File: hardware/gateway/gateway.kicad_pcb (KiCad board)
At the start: 2 copper layers, 65 x 32 mm, 34 parts, among them J1 FTDI, J2 Conn_Coaxial, J3 Raspberry_Pi_2_3, U1 RFM69HW, U2 MCP7940N-xSN, U3 AP130-xxY, Y1 32768 - 6pF

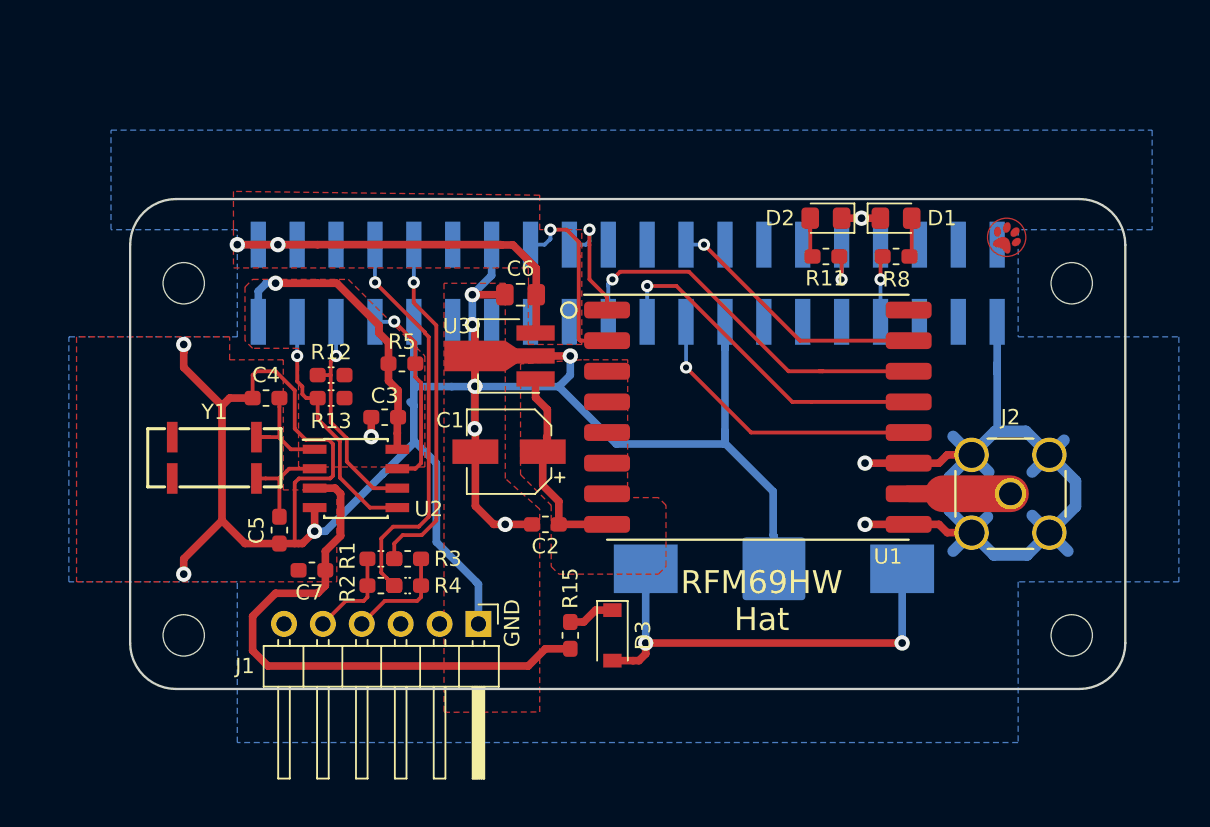
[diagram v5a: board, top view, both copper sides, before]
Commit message: DS1307 and PTH crystal
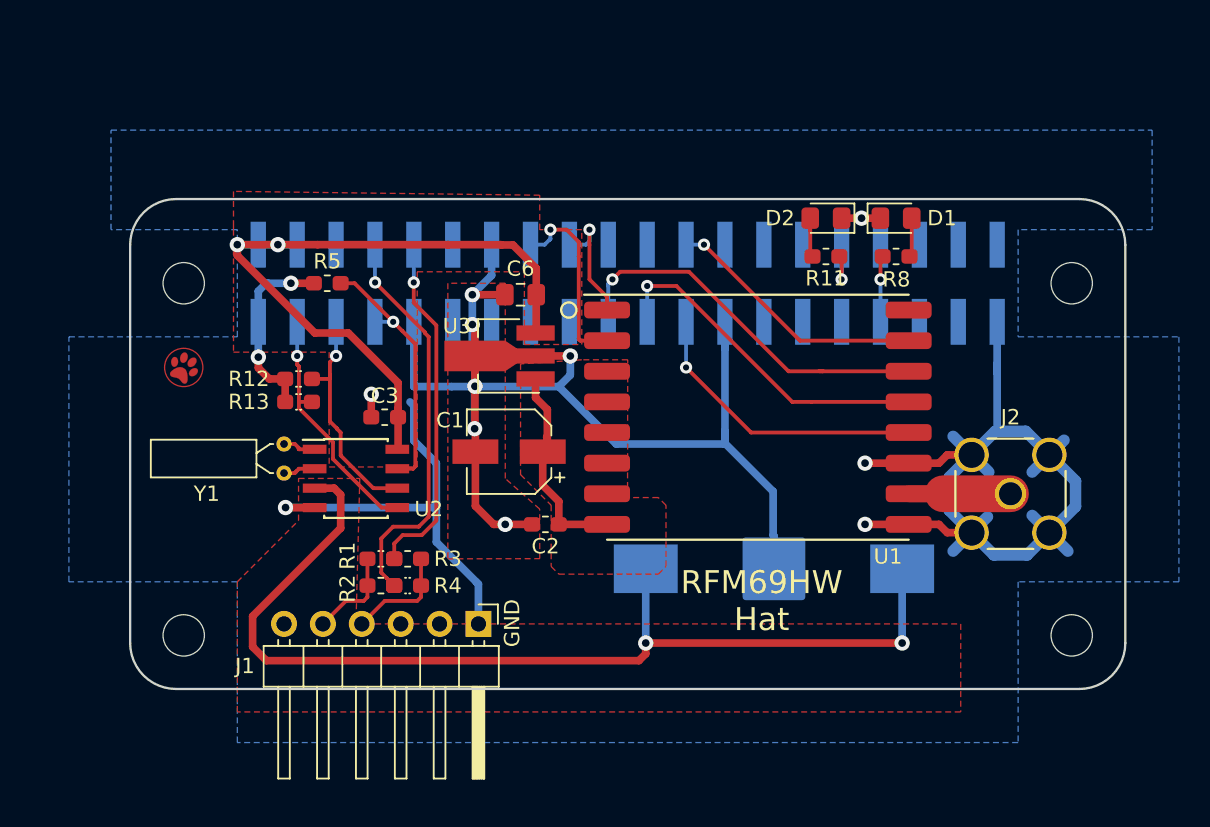
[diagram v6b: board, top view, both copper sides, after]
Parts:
- removed C4, C5: 10p, Capacitor_SMD:C_0603_1608Metric_Pad1.05x0.95mm_HandSolder
- removed C7: 100n, Capacitor_SMD:C_0603_1608Metric_Pad1.05x0.95mm_HandSolder
- removed D3: B0520LW-7-F, Diode_SMD:D_SOD-123
- removed R15: 1k, Resistor_SMD:R_0603_1608Metric_Pad1.05x0.95mm_HandSolder
- U2: value MCP7940N-xSN -> DS1307Z+
- Y1: value 32768 - 6pF -> 32768; footprint humidity:Crystal LFXTAL016178 -> Crystal:Crystal_C26-LF_D2.1mm_L6.5mm_Horizontal
- moved G*** 54.4 mm to (100.0, 55.5)
- moved R5 7.16 mm to (109.4, 50.0)
- moved Y1 4.64 mm to (106.5, 60.5), turned to 270 degrees
- moved R12 2.14 mm to (107.5, 56.2), turned to 180 degrees
- moved R13 2.14 mm to (107.5, 57.8), turned to 180 degrees
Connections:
- net /MFP renamed /RTC_SQ_OUT
- BT1 pad 1: /VBAT_IN -> /VBAT
- C3 pad 1: +3V3_PI -> +5V_PI
- U2 pad 8: +3V3_PI -> +5V_PI
- Y1 pad 1: /X2 -> /X1
- Y1 pad 2: /X1 -> /X2
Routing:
- net GND: track 226.1 -> 180.7 mm, vias 13 -> 11
- net /VBAT: track 37.7 -> 67.6 mm, vias 0 -> 2
- net /VBAT_IN: track 29.5 -> 0.00 mm, vias 2 -> 0
- net +5V_PI: track 28.4 -> 47.4 mm
- net +3V3_PI: track 20.0 -> 12.5 mm, vias 1 -> 2
- net /X1: track 7.58 -> 2.19 mm
- net /X2: track 6.56 -> 2.13 mm
- net /RTC_SQ_OUT: track 12.9 -> 16.9 mm
- net /VBAT_D: track 3.07 -> 0.00 mm
- net /SCL: track 14.6 -> 15.2 mm
- added copper zone on F.Cu, net /VBAT
- removed copper zone on F.Cu, net +3V3_PI

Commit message: Minor layout adjustments
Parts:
- moved BT1 4.55 mm to (134.0, 68.8)
- moved G*** 3.25 mm to (115.2, 62.2)
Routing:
- net /VBAT: track 67.6 -> 5.00 mm
- net /MISO: track 22.6 -> 19.3 mm
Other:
- board text added: "OOS 2019-06-24"
- board text removed: "OOS 2019-06-13"

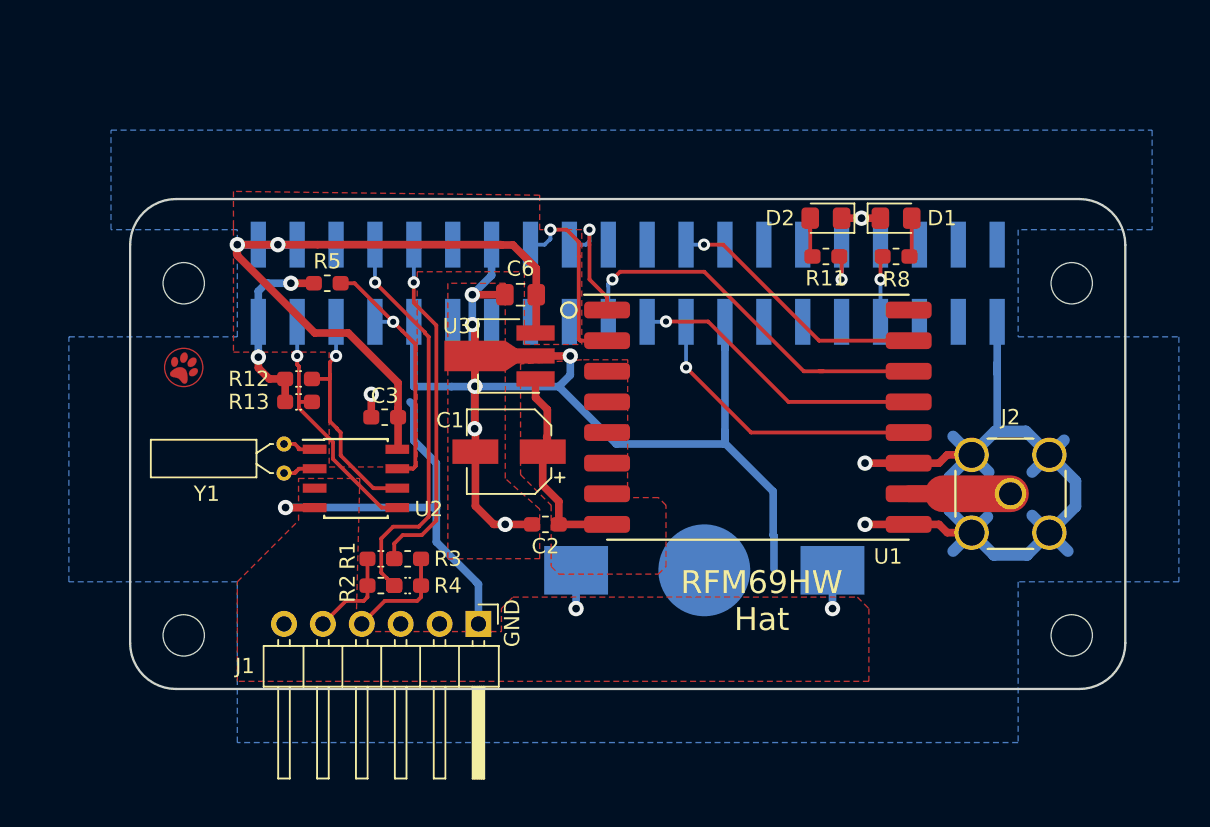
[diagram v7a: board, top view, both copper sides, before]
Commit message: Adjusted CR1216 footprint
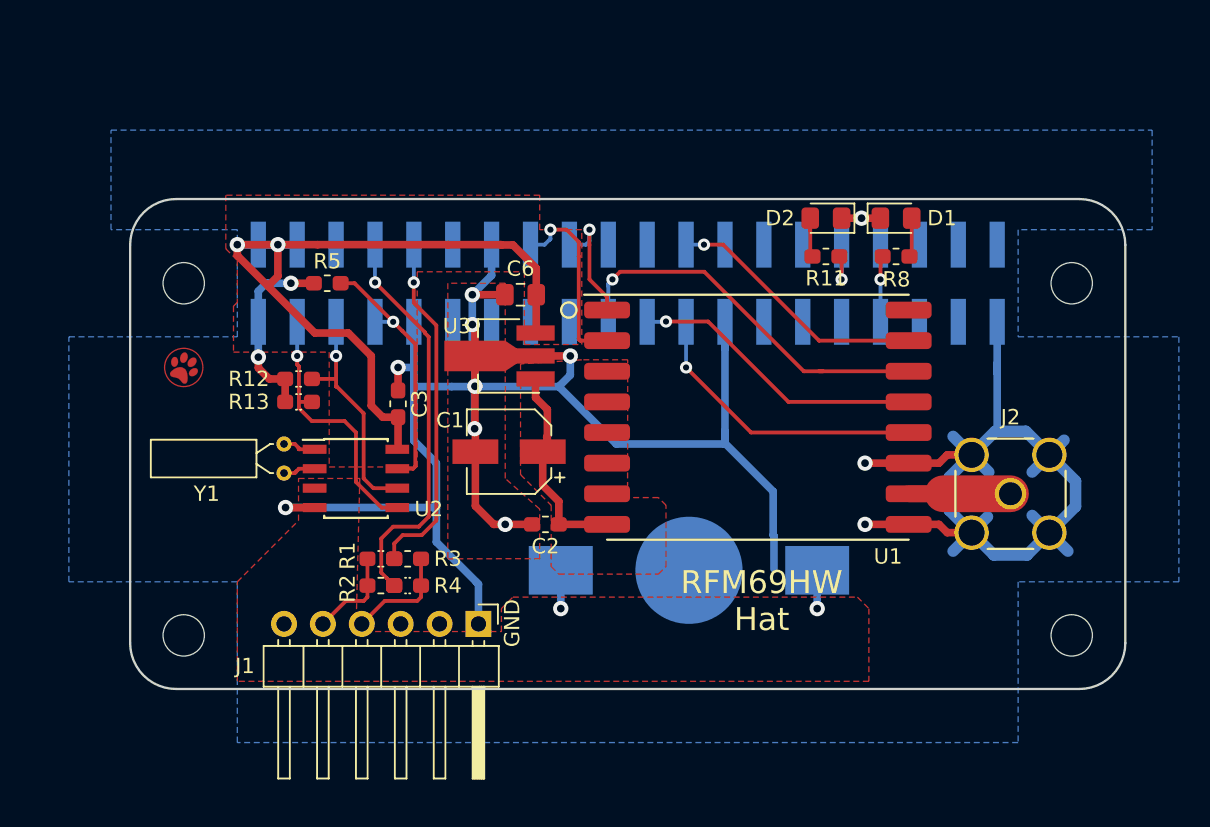
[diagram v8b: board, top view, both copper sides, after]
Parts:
- moved C3 1.24 mm to (114.0, 57.9), turned to 90 degrees
- moved BT1 1.00 mm to (133.0, 68.8)
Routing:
- net +5V_PI: track 47.4 -> 50.9 mm
- net GND: track 180.7 -> 182.6 mm
- net /SDA: track 16.3 -> 17.6 mm
